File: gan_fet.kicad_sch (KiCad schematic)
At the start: 6 parts, among them J1 Conn_01x04_Male, Q1 EPC2036, U1 NPC81074

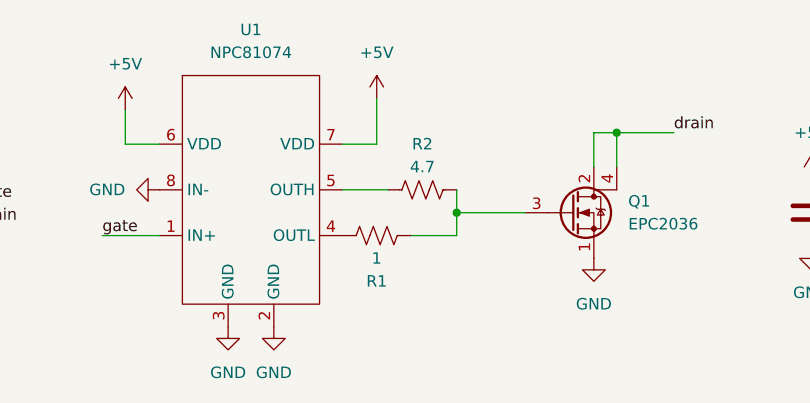
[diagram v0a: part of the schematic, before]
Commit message: layout changes
rotate fet 45 degrees
fills/vias for GND and Drain
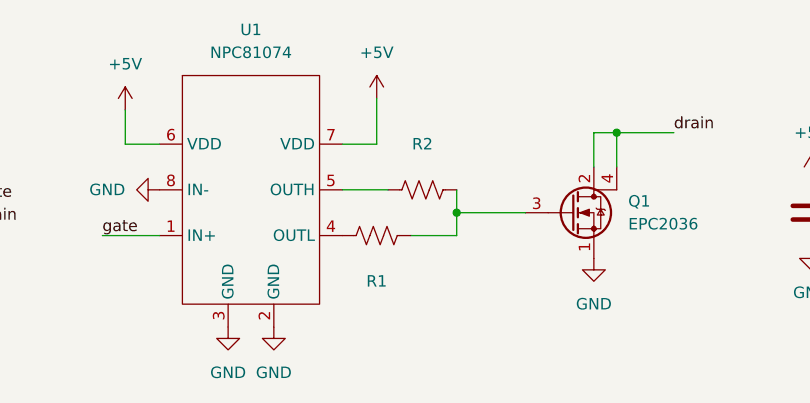
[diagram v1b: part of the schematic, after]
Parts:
- R1: value 1 -> (none); footprint Resistor_SMD:R_0603_1608Metric -> (none)
- R2: value 4.7 -> (none); footprint Resistor_SMD:R_0603_1608Metric -> (none)
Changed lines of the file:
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@@
     (in_bom yes) (on_board yes)
     (property "Reference" "R1" (id 0) (at 111.76 97.79 90))
-    (property "Value" "1" (id 1) (at 111.76 95.25 90))
-    (property "Footprint" "Resistor_SMD:R_0603_1608Metric" (id 2) (at 112.014 91.694 90)
+    (property "Value" "" (id 1) (at 111.76 95.25 90))
+    (property "Footprint" "" (id 2) (at 112.014 91.694 90)
       (effects (font (size 1.27 1.27)) hide)
     )
@@
     (in_bom yes) (on_board yes)
     (property "Reference" "R2" (id 0) (at 116.84 82.55 90))
-    (property "Value" "4.7" (id 1) (at 116.84 85.09 90))
-    (property "Footprint" "Resistor_SMD:R_0603_1608Metric" (id 2) (at 117.094 86.614 90)
+    (property "Value" "" (id 1) (at 116.84 85.09 90))
+    (property "Footprint" "" (id 2) (at 117.094 86.614 90)
       (effects (font (size 1.27 1.27)) hide)
     )
@@
     )
     (path "/95897ce4-9ee1-47ce-848a-22ccb1db8f84"
-      (reference "R1") (unit 1) (value "1") (footprint "Resistor_SMD:R_0603_1608Metric")
+      (reference "R1") (unit 1) (value "1") (footprint "Resistor_SMD:R_0805_2012Metric_Pad1.20x1.40mm_HandSolder")
     )
     (path "/bf442f9e-bd41-4738-8581-e2e0724c0986"
-      (reference "R2") (unit 1) (value "4.7") (footprint "Resistor_SMD:R_0603_1608Metric")
+      (reference "R2") (unit 1) (value "4.7") (footprint "Resistor_SMD:R_0805_2012Metric_Pad1.20x1.40mm_HandSolder")
     )
     (path "/6718bb7e-e527-407f-97e8-371aa92ae69d"

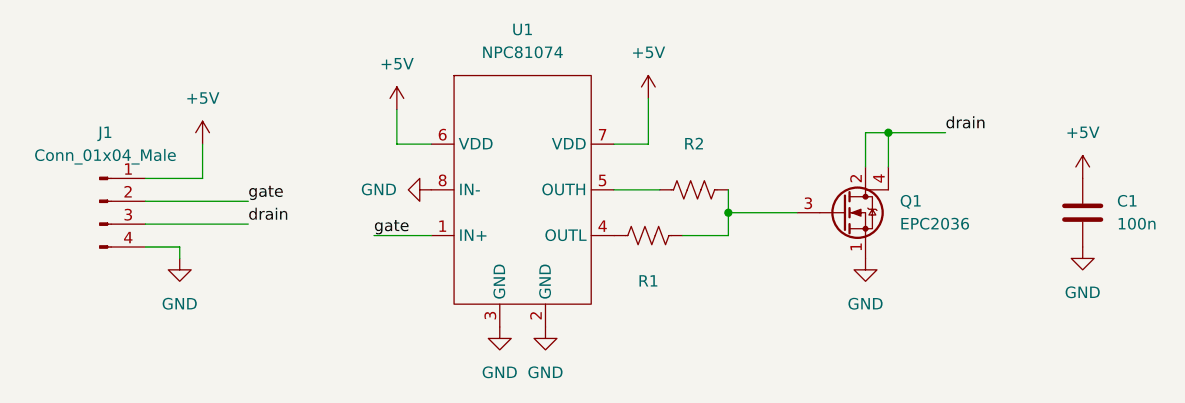
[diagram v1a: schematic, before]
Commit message: changed pinout, updated EPC footprint
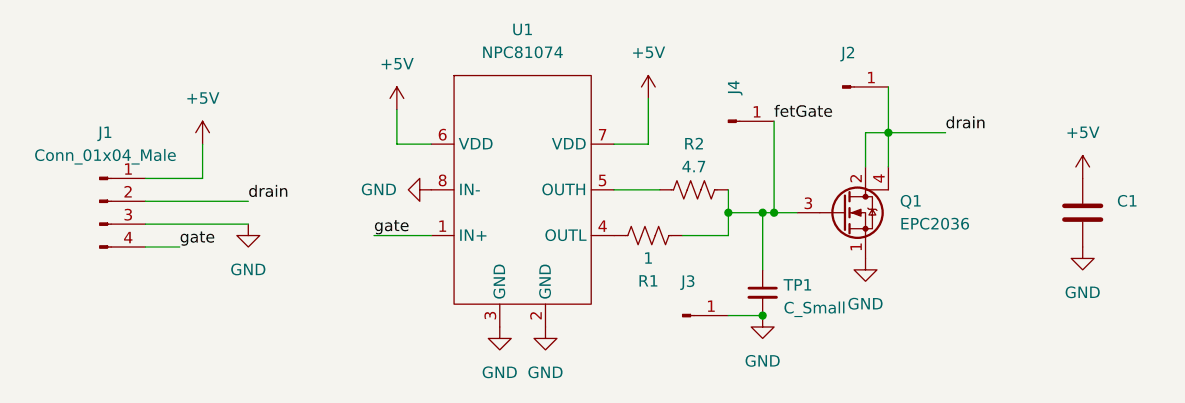
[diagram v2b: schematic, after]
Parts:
- added J2, J3, J4: (no value), symbol Connector:Conn_01x01_Male
- added TP1: C_Small, Resistor_SMD:R_1206_3216Metric, symbol Device:C_Small
- C1: value 100n -> (none); footprint Capacitor_SMD:C_0603_1608Metric -> (none)
- R1: value (none) -> 1; footprint (none) -> Resistor_SMD:R_0805_2012Metric_Pad1.20x1.40mm_HandSolder
- R2: value (none) -> 4.7; footprint (none) -> Resistor_SMD:R_0805_2012Metric_Pad1.20x1.40mm_HandSolder
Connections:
- net GND: now also J1.3 (Pin_3), J3.1 (Pin_1), TP1.2; no longer J1.4 (Pin_4)
- net drain: now also J1.2 (Pin_2), J2.1 (Pin_1); no longer J1.3 (Pin_3)
- net gate: now also J1.4 (Pin_4); no longer J1.2 (Pin_2)
- net fetGate: now reaches Q1.3 (G), R1.2, R2.2
- net fetGate: now also J4.1 (Pin_1), TP1.1
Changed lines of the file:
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@@
 (kicad_sch (version 20211123) (generator eeschema)
   (paper "A4")
+  (junction (at 124.46 101.6) (diameter 0) (color 0 0 0 0)
+  )
+  (junction (at 125.73 90.17) (diameter 0) (color 0 0 0 0)
+  )
   (junction (at 120.65 90.17) (diameter 0) (color 0 0 0 0)
   )
+  (junction (at 124.46 90.17) (diameter 0) (color 0 0 0 0)
+  )
   (junction (at 138.43 81.28) (diameter 0) (color 0 0 0 0)
   )
@@
     (stroke (width 0) (type default) (color 0 0 0 0))
   )
-  (wire (pts (xy 120.65 90.17) (xy 128.27 90.17))
+  (wire (pts (xy 120.65 90.17) (xy 124.46 90.17))
     (stroke (width 0) (type default) (color 0 0 0 0))
   )
@@
     (stroke (width 0) (type default) (color 0 0 0 0))
   )
-  (wire (pts (xy 59.69 95.25) (xy 59.69 93.98))
+  (wire (pts (xy 124.46 90.17) (xy 124.46 96.52))
     (stroke (width 0) (type default) (color 0 0 0 0))
   )
@@
     (stroke (width 0) (type default) (color 0 0 0 0))
   )
+  (wire (pts (xy 120.65 101.6) (xy 124.46 101.6))
+    (stroke (width 0) (type default) (color 0 0 0 0))
+  )
   (wire (pts (xy 115.57 92.71) (xy 120.65 92.71))
     (stroke (width 0) (type default) (color 0 0 0 0))
   )
+  (wire (pts (xy 138.43 76.2) (xy 138.43 81.28))
+    (stroke (width 0) (type default) (color 0 0 0 0))
+  )
   (wire (pts (xy 83.82 78.74) (xy 83.82 82.55))
     (stroke (width 0) (type default) (color 0 0 0 0))
   )
+  (wire (pts (xy 125.73 80.01) (xy 125.73 90.17))
+    (stroke (width 0) (type default) (color 0 0 0 0))
+  )
+  (wire (pts (xy 124.46 90.17) (xy 125.73 90.17))
+    (stroke (width 0) (type default) (color 0 0 0 0))
+  )
   (wire (pts (xy 135.89 81.28) (xy 138.43 81.28))
     (stroke (width 0) (type default) (color 0 0 0 0))
@@
     (stroke (width 0) (type default) (color 0 0 0 0))
   )
+  (wire (pts (xy 125.73 90.17) (xy 128.27 90.17))
+    (stroke (width 0) (type default) (color 0 0 0 0))
+  )
   (wire (pts (xy 59.69 93.98) (xy 55.88 93.98))
     (stroke (width 0) (type default) (color 0 0 0 0))
@@
   (wire (pts (xy 62.23 86.36) (xy 55.88 86.36))
     (stroke (width 0) (type default) (color 0 0 0 0))
+  )
+  (label "gate" (at 59.69 93.98 0)
+    (effects (font (size 1.27 1.27)) (justify left bottom))
+  )
+  (label "fetGate" (at 125.73 80.01 0)
+    (effects (font (size 1.27 1.27)) (justify left bottom))
   )
   (label "gate" (at 81.28 92.71 0)
     (effects (font (size 1.27 1.27)) (justify left bottom))
   )
-  (label "drain" (at 67.31 91.44 0)
-    (effects (font (size 1.27 1.27)) (justify left bottom))
-  )
-  (label "gate" (at 67.31 88.9 0)
+  (label "drain" (at 67.31 88.9 0)
     (effects (font (size 1.27 1.27)) (justify left bottom))
   )
@@
     (pin "1")
   )
+  (symbol (lib_id "Device:C_Small") (at 124.46 99.06 0) (unit 1)
+    (in_bom yes) (on_board yes) (fields_autoplaced)
+    (property "Reference" "TP1" (id 0) (at 126.7841 98.2316 0)
+      (effects (font (size 1.27 1.27)) (justify left))
+    )
+    (property "Value" "C_Small" (id 1) (at 126.7841 100.7685 0)
+      (effects (font (size 1.27 1.27)) (justify left))
+    )
+    (property "Footprint" "Resistor_SMD:R_1206_3216Metric" (id 2) (at 124.46 99.06 0)
+      (effects (font (size 1.27 1.27)) hide)
+    )
+    (property "Datasheet" "~" (id 3) (at 124.46 99.06 0)
+      (effects (font (size 1.27 1.27)) hide)
+    )
+    (pin "1")
+    (pin "2")
+  )
   (symbol (lib_id "power:GND") (at 100.33 102.87 0) (unit 1)
     (in_bom yes) (on_board yes) (fields_autoplaced)
@@
     (pin "1")
   )
-  (symbol (lib_id "power:GND") (at 59.69 95.25 0) (unit 1)
-    (in_bom yes) (on_board yes) (fields_autoplaced)
-    (property "Reference" "#PWR01" (id 0) (at 59.69 101.6 0)
-      (effects (font (size 1.27 1.27)) hide)
-    )
-    (property "Value" "GND" (id 1) (at 59.69 100.33 0))
-    (property "Footprint" "" (id 2) (at 59.69 95.25 0)
-      (effects (font (size 1.27 1.27)) hide)
-    )
-    (property "Datasheet" "" (id 3) (at 59.69 95.25 0)
+  (symbol (lib_id "power:GND") (at 67.31 91.44 0) (unit 1)
+    (in_bom yes) (on_board yes) (fields_autoplaced)
+    (property "Reference" "#PWR01" (id 0) (at 67.31 97.79 0)
+      (effects (font (size 1.27 1.27)) hide)
+    )
+    (property "Value" "GND" (id 1) (at 67.31 96.52 0))
+    (property "Footprint" "" (id 2) (at 67.31 91.44 0)
+      (effects (font (size 1.27 1.27)) hide)
+    )
+    (property "Datasheet" "" (id 3) (at 67.31 91.44 0)
+      (effects (font (size 1.27 1.27)) hide)
+    )
+    (pin "1")
+  )
+  (symbol (lib_id "Connector:Conn_01x01_Male") (at 133.35 76.2 0) (unit 1)
+    (in_bom yes) (on_board yes) (fields_autoplaced)
+    (property "Reference" "J2" (id 0) (at 133.985 72.424 0))
+    (property "Value" "" (id 1) (at 133.985 74.9609 0))
+    (property "Footprint" "" (id 2) (at 133.35 76.2 0)
+      (effects (font (size 1.27 1.27)) hide)
+    )
+    (property "Datasheet" "~" (id 3) (at 133.35 76.2 0)
       (effects (font (size 1.27 1.27)) hide)
     )
@@
     (pin "8")
   )
+  (symbol (lib_id "Connector:Conn_01x01_Male") (at 115.57 101.6 0) (unit 1)
+    (in_bom yes) (on_board yes) (fields_autoplaced)
+    (property "Reference" "J3" (id 0) (at 116.205 97.824 0))
+    (property "Value" "" (id 1) (at 116.205 100.3609 0))
+    (property "Footprint" "" (id 2) (at 115.57 101.6 0)
+      (effects (font (size 1.27 1.27)) hide)
+    )
+    (property "Datasheet" "~" (id 3) (at 115.57 101.6 0)
+      (effects (font (size 1.27 1.27)) hide)
+    )
+    (pin "1")
+  )
+  (symbol (lib_id "Connector:Conn_01x01_Male") (at 120.65 80.01 0) (unit 1)
+    (in_bom yes) (on_board yes)
+    (property "Reference" "J4" (id 0) (at 121.285 76.234 90))
+    (property "Value" "" (id 1) (at 121.285 78.7709 0))
+    (property "Footprint" "" (id 2) (at 120.65 80.01 0)
+      (effects (font (size 1.27 1.27)) hide)
+    )
+    (property "Datasheet" "~" (id 3) (at 120.65 80.01 0)
+      (effects (font (size 1.27 1.27)) hide)
+    )
+    (pin "1")
+  )
   (symbol (lib_id "Device:Q_NMOS_SDGD") (at 133.35 90.17 0) (unit 1)
     (in_bom yes) (on_board yes) (fields_autoplaced)
@@
     (pin "3")
     (pin "4")
+  )
+  (symbol (lib_id "power:GND") (at 124.46 101.6 0) (unit 1)
+    (in_bom yes) (on_board yes) (fields_autoplaced)
+    (property "Reference" "#PWR0101" (id 0) (at 124.46 107.95 0)
+      (effects (font (size 1.27 1.27)) hide)
+    )
+    (property "Value" "GND" (id 1) (at 124.46 106.68 0))
+    (property "Footprint" "" (id 2) (at 124.46 101.6 0)
+      (effects (font (size 1.27 1.27)) hide)
+    )
+    (property "Datasheet" "" (id 3) (at 124.46 101.6 0)
+      (effects (font (size 1.27 1.27)) hide)
+    )
+    (pin "1")
   )
   (symbol (lib_id "Device:R_US") (at 111.76 92.71 90) (unit 1)
     (in_bom yes) (on_board yes)
     (property "Reference" "R1" (id 0) (at 111.76 97.79 90))
-    (property "Value" "" (id 1) (at 111.76 95.25 90))
-    (property "Footprint" "" (id 2) (at 112.014 91.694 90)
+    (property "Value" "1" (id 1) (at 111.76 95.25 90))
+    (property "Footprint" "Resistor_SMD:R_0805_2012Metric_Pad1.20x1.40mm_HandSolder" (id 2) (at 112.014 91.694 90)
       (effects (font (size 1.27 1.27)) hide)
     )
@@
       (effects (font (size 1.27 1.27)) (justify left))
     )
-    (property "Value" "100n" (id 1) (at 163.83 91.4399 0)
-      (effects (font (size 1.27 1.27)) (justify left))
-    )
-    (property "Footprint" "Capacitor_SMD:C_0603_1608Metric" (id 2) (at 160.9852 93.98 0)
+    (property "Value" "" (id 1) (at 163.83 91.4399 0)
+      (effects (font (size 1.27 1.27)) (justify left))
+    )
+    (property "Footprint" "" (id 2) (at 160.9852 93.98 0)
       (effects (font (size 1.27 1.27)) hide)
     )
@@
     (in_bom yes) (on_board yes)
     (property "Reference" "R2" (id 0) (at 116.84 82.55 90))
-    (property "Value" "" (id 1) (at 116.84 85.09 90))
-    (property "Footprint" "" (id 2) (at 117.094 86.614 90)
+    (property "Value" "4.7" (id 1) (at 116.84 85.09 90))
+    (property "Footprint" "Resistor_SMD:R_0805_2012Metric_Pad1.20x1.40mm_HandSolder" (id 2) (at 117.094 86.614 90)
       (effects (font (size 1.27 1.27)) hide)
     )
@@
       (reference "#PWR010") (unit 1) (value "GND") (footprint "")
     )
+    (path "/946871db-eacd-47b0-9152-335749d901bc"
+      (reference "#PWR0101") (unit 1) (value "GND") (footprint "")
+    )
     (path "/98e3f34b-2f01-4d8f-9716-13fb375a8535"
-      (reference "C1") (unit 1) (value "100n") (footprint "Capacitor_SMD:C_0603_1608Metric")
+      (reference "C1") (unit 1) (value "100n") (footprint "Capacitor_SMD:C_1206_3216Metric")
     )
     (path "/d708cbbc-7fcd-4298-8fa3-559ae97654db"
       (reference "J1") (unit 1) (value "Conn_01x04_Male") (footprint "Connector_PinHeader_2.54mm:PinHeader_1x04_P2.54mm_Horizontal")
     )
+    (path "/490e8ab6-4c52-4f22-9844-418e6b76f8c7"
+      (reference "J2") (unit 1) (value "D") (footprint "Connector_Pin:Pin_D1.0mm_L10.0mm")
+    )
+    (path "/77320cbf-7898-4a50-9ca9-25795e54086e"
+      (reference "J3") (unit 1) (value "S") (footprint "Connector_Pin:Pin_D1.0mm_L10.0mm")
+    )
+    (path "/8bea086a-74ce-4f77-8026-cb3925c0b063"
+      (reference "J4") (unit 1) (value "G") (footprint "Connector_Pin:Pin_D1.0mm_L10.0mm")
+    )
     (path "/91471996-4c6d-485e-b448-6904dece7e73"
       (reference "Q1") (unit 1) (value "EPC2036") (footprint "epc:epc2036")
@@
       (reference "R2") (unit 1) (value "4.7") (footprint "Resistor_SMD:R_0805_2012Metric_Pad1.20x1.40mm_HandSolder")
     )
+    (path "/151e5bea-598b-4a84-9928-2b2d6b1d9376"
+      (reference "TP1") (unit 1) (value "C_Small") (footprint "Resistor_SMD:R_1206_3216Metric")
+    )
     (path "/6718bb7e-e527-407f-97e8-371aa92ae69d"

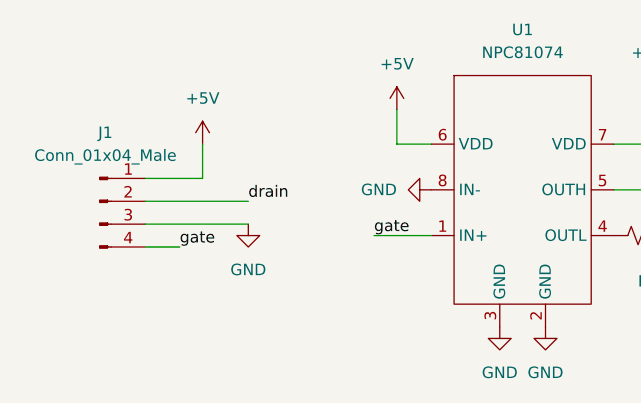
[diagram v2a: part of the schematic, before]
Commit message: FET to backside, added PTH for BS170 pinout now matches IRF510 better EPC2036 footprint (pad and mask)
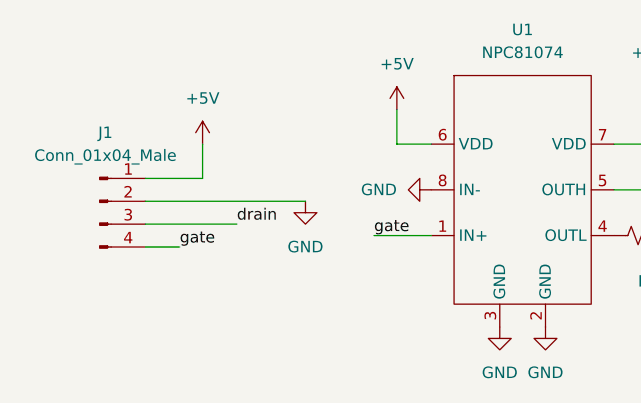
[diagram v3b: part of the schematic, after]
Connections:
- net GND: now also J1.2 (Pin_2); no longer J1.3 (Pin_3)
- net drain: now also J1.3 (Pin_3); no longer J1.2 (Pin_2)
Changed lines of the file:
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@@
+    (stroke (width 0) (type default) (color 0 0 0 0))
+  )
+  (wire (pts (xy 55.88 91.44) (xy 66.04 91.44))
     (stroke (width 0) (type default) (color 0 0 0 0))
   )
@@
     (stroke (width 0) (type default) (color 0 0 0 0))
   )
+  (wire (pts (xy 55.88 88.9) (xy 73.66 88.9))
+    (stroke (width 0) (type default) (color 0 0 0 0))
+  )
   (wire (pts (xy 124.46 90.17) (xy 125.73 90.17))
     (stroke (width 0) (type default) (color 0 0 0 0))
   )
   (wire (pts (xy 135.89 81.28) (xy 138.43 81.28))
-    (stroke (width 0) (type default) (color 0 0 0 0))
-  )
-  (wire (pts (xy 55.88 91.44) (xy 67.31 91.44))
-    (stroke (width 0) (type default) (color 0 0 0 0))
-  )
-  (wire (pts (xy 67.31 88.9) (xy 55.88 88.9))
     (stroke (width 0) (type default) (color 0 0 0 0))
   )
@@
     (effects (font (size 1.27 1.27)) (justify left bottom))
   )
-  (label "drain" (at 67.31 88.9 0)
+  (label "drain" (at 66.04 91.44 0)
     (effects (font (size 1.27 1.27)) (justify left bottom))
   )
@@
     (pin "1")
   )
-  (symbol (lib_id "power:GND") (at 67.31 91.44 0) (unit 1)
+  (symbol (lib_id "power:GND") (at 73.66 88.9 0) (unit 1)
     (in_bom yes) (on_board yes) (fields_autoplaced)
-    (property "Reference" "#PWR01" (id 0) (at 67.31 97.79 0)
+    (property "Reference" "#PWR01" (id 0) (at 73.66 95.25 0)
       (effects (font (size 1.27 1.27)) hide)
     )
-    (property "Value" "GND" (id 1) (at 67.31 96.52 0))
-    (property "Footprint" "" (id 2) (at 67.31 91.44 0)
+    (property "Value" "GND" (id 1) (at 73.66 93.98 0))
+    (property "Footprint" "" (id 2) (at 73.66 88.9 0)
       (effects (font (size 1.27 1.27)) hide)
     )
-    (property "Datasheet" "" (id 3) (at 67.31 91.44 0)
+    (property "Datasheet" "" (id 3) (at 73.66 88.9 0)
       (effects (font (size 1.27 1.27)) hide)
     )

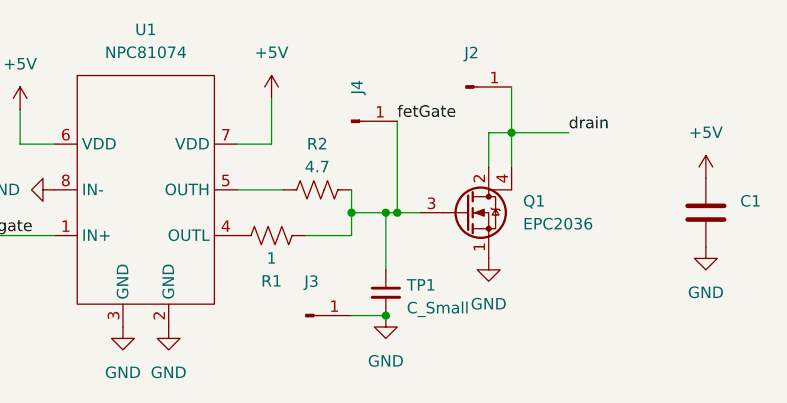
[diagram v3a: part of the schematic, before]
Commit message: Rev0 board to JLCPCB
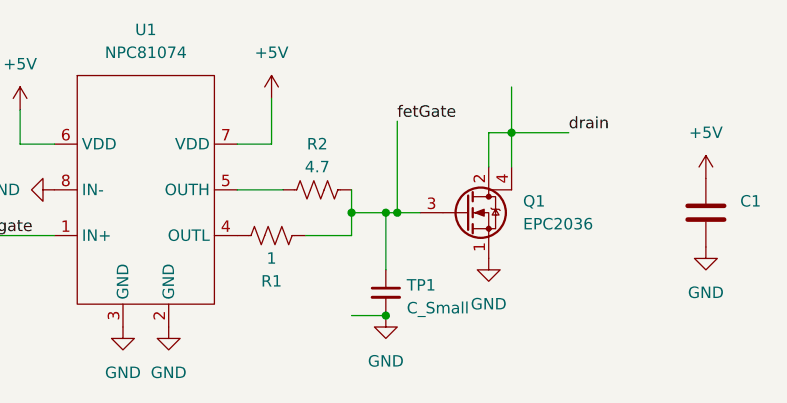
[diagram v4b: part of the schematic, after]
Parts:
- removed J2, J3, J4: (no value), symbol Connector:Conn_01x01_Male
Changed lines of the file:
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@@
-    (pin "1")
-  )
-  (symbol (lib_id "Connector:Conn_01x01_Male") (at 133.35 76.2 0) (unit 1)
-    (in_bom yes) (on_board yes) (fields_autoplaced)
-    (property "Reference" "J2" (id 0) (at 133.985 72.424 0))
-    (property "Value" "" (id 1) (at 133.985 74.9609 0))
-    (property "Footprint" "" (id 2) (at 133.35 76.2 0)
-      (effects (font (size 1.27 1.27)) hide)
-    )
-    (property "Datasheet" "~" (id 3) (at 133.35 76.2 0)
-      (effects (font (size 1.27 1.27)) hide)
-    )
     (pin "1")
   )
@@
     (pin "8")
   )
-  (symbol (lib_id "Connector:Conn_01x01_Male") (at 115.57 101.6 0) (unit 1)
-    (in_bom yes) (on_board yes) (fields_autoplaced)
-    (property "Reference" "J3" (id 0) (at 116.205 97.824 0))
-    (property "Value" "" (id 1) (at 116.205 100.3609 0))
-    (property "Footprint" "" (id 2) (at 115.57 101.6 0)
-      (effects (font (size 1.27 1.27)) hide)
-    )
-    (property "Datasheet" "~" (id 3) (at 115.57 101.6 0)
-      (effects (font (size 1.27 1.27)) hide)
-    )
-    (pin "1")
-  )
-  (symbol (lib_id "Connector:Conn_01x01_Male") (at 120.65 80.01 0) (unit 1)
-    (in_bom yes) (on_board yes)
-    (property "Reference" "J4" (id 0) (at 121.285 76.234 90))
-    (property "Value" "" (id 1) (at 121.285 78.7709 0))
-    (property "Footprint" "" (id 2) (at 120.65 80.01 0)
-      (effects (font (size 1.27 1.27)) hide)
-    )
-    (property "Datasheet" "~" (id 3) (at 120.65 80.01 0)
-      (effects (font (size 1.27 1.27)) hide)
-    )
-    (pin "1")
-  )
   (symbol (lib_id "Device:Q_NMOS_SDGD") (at 133.35 90.17 0) (unit 1)
     (in_bom yes) (on_board yes) (fields_autoplaced)
@@
       (reference "J1") (unit 1) (value "Conn_01x04_Male") (footprint "Connector_PinHeader_2.54mm:PinHeader_1x04_P2.54mm_Horizontal")
     )
-    (path "/490e8ab6-4c52-4f22-9844-418e6b76f8c7"
-      (reference "J2") (unit 1) (value "D") (footprint "Connector_Pin:Pin_D1.0mm_L10.0mm")
-    )
-    (path "/77320cbf-7898-4a50-9ca9-25795e54086e"
-      (reference "J3") (unit 1) (value "S") (footprint "Connector_Pin:Pin_D1.0mm_L10.0mm")
-    )
-    (path "/8bea086a-74ce-4f77-8026-cb3925c0b063"
-      (reference "J4") (unit 1) (value "G") (footprint "Connector_Pin:Pin_D1.0mm_L10.0mm")
-    )
     (path "/91471996-4c6d-485e-b448-6904dece7e73"
